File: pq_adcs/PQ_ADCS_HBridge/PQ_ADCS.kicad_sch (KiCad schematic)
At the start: 48 parts, among them J1 CES-110-02-L-S, J10 Pico-Clasp_01x09, J11 Pico-Clasp_01x15, J12 CES-102-02-L-S, J2 CES-110-02-L-S, J3 CES-110-02-L-S, J4 CES-110-02-L-S, J5 Pico-Clasp_01x03, J6 Pico-Clasp_01x10, J7 Pico-Clasp_01x10, J8 Pico-Clasp_01x10, J9 Pico-Clasp_01x10, U1 LPV542, U2 LPV542, U3 LPV542, U4 IIM-42652, U5 DRV8214RTER, U6 TMUX1108RSVR, U7 MMC5983MA

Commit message: H-Bridge Chips Update
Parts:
- added U8, U9: DRV8214RTER, DRV8214RTER:IC_DRV8214RTER, symbol DRV8214RTER:DRV8214RTER
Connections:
- net MAG+X is gone; now on net +MAG+X: J7.2
- net 3V3_PERM: now also U5.16 (VREF), U8.16 (VREF), U8.2 (VCC), U9.16 (VREF), U9.2 (VCC)
- net ADCS_POWER: now also U8.11 (~{SLEEP}), U9.11 (~{SLEEP})
- net GND: now also U5.17 (EXP), U5.3 (RC_OUT), U5.4 (~{FAULT}), U8.12 (PH/IN2), U8.13 (EN/IN1), U8.17 (EXP), U8.3 (RC_OUT), U8.4 (~{FAULT}), U8.7 (GND), U9.12 (PH/IN2), U9.13 (EN/IN1), U9.17 (EXP), U9.3 (RC_OUT), U9.4 (~{FAULT}), U9.7 (GND)
- net SCL3: now also U8.15 (SCL), U9.15 (SCL)
- net SDA3: now also U8.14 (SDA), U9.14 (SDA)
- net +MAG+X: now reaches U5.6 (OUT1)
- net -MAG-X: now reaches U5.8 (OUT2)
- net -MAG-X: now also J6.3
- net MAG+Y renamed +MAG+Y
- net +MAG+Y: now also U8.6 (OUT1)
- net MAG+Z renamed +MAG+Z
- net +MAG+Z: now also U9.6 (OUT1)
- net MAG-X renamed +MAG-X
- net MAG-Y renamed +MAG-Y
- net MAG-Z renamed +MAG-Z
- removed net VCC_MAG: J11.3, J12.1, J6.3, J7.3, J8.3, J9.3
- new net -MAG+X: J7.3
- new net -MAG+Y: J12.1
- new net -MAG+Z: J9.3
- new net -MAG-Y: J11.3, U8.8 (OUT2)
- new net -MAG-Z: J8.3, U9.8 (OUT2)
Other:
- moved on the sheet: U5

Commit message: PCB Update
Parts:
- added R13, R14, R15: 22k, Resistor_SMD:R_0603_1608Metric, symbol Device:R
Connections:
- net 3V3_PERM: now also U5.5 (VM), U8.5 (VM), U9.5 (VM)
- net GND: now also U5.10 (A0), U5.9 (A1), U8.10 (A0), R13.2, R14.2, R15.2
- net at U9.1 (IPROPI): now also R15.1
- net at U8.1 (IPROPI): now also R14.1
- net at U5.1 (IPROPI): now also R13.1
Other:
- note added: "I2C address: 0000b"
- note added: "I2C address: 0001b"
- note added: "I2C address: 0100b"
- note removed: "I2C address:"

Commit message: Reduced errors
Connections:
- net PHT5_ADCS: now also C6.2, R12.1
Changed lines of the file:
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@@
+	(wire
+		(pts
+			(xy 212.09 116.84) (xy 248.92 116.84)
+		)
+		(stroke
+			(width 0)
+			(type default)
+		)
+	)
 	(wire
 		(pts

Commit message: Restart
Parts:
- removed R13, R14, R15: 22k, Resistor_SMD:R_0603_1608Metric, symbol Device:R
- removed U5, U8, U9: DRV8214RTER, DRV8214RTER:IC_DRV8214RTER, symbol DRV8214RTER:DRV8214RTER
- added C11: 100 nF, Capacitor_SMD:C_0603_1608Metric, symbol Device:C
- added C13, C14: 1 uF, Capacitor_SMD:C_0603_1608Metric, symbol Device:C
- added U5: BD2606MVV, Package_DFN_QFN:QFN-16-1EP_4x4mm_P0.65mm_EP2.5x2.5mm, symbol power-nsl:BD2606MVV
- renumbered U1 to U
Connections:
- net -MAG+Y is gone; now on net VCC_MAG: J12.1
- net -MAG+Z is gone; now on net VCC_MAG: J9.3
- net -MAG-X is gone; now on net VCC_MAG: J6.3
- net -MAG-Y is gone; now on net VCC_MAG: J11.3
- net -MAG-Z is gone; now on net VCC_MAG: J8.3
- net ADCS_POWER: now also C11.1, U5.4 (EN), U5.6 (IN)
- net GND: now also C11.2, U5.11 (GND), U5.17 (EPAD)
- net PHT5_ADCS: no longer C6.2, R12.1, U3.7 (OUT_B), U6.9 (S6)
- net SCL3: now also U5.3 (SCL)
- net SDA3: now also U5.2 (SDA)
- net +MAG+X renamed MAG+X
- net MAG+X: now also U5.16 (LEDA2)
- net +MAG+Y renamed MAG+Y
- net MAG+Y: now also U5.12 (LEDC2)
- net +MAG+Z renamed MAG+Z
- net MAG+Z: now also U5.14 (LEDB2)
- net +MAG-X renamed MAG-X
- net MAG-X: now also U5.1 (LEDA1)
- net +MAG-Y renamed MAG-Y
- net MAG-Y: now also U5.13 (LEDC1)
- net +MAG-Z renamed MAG-Z
- net MAG-Z: now also U5.15 (LEDB1)
- net -MAG+X renamed VCC_MAG
- net VCC_MAG: now also U5.5 (OUT)
- new net: C13.1, U5.10 (C2P)
- new net: C13.2, U5.9 (C2N)
- new net: C14.1, U5.8 (C1P)
- new net: C14.2, U5.7 (C1N)
- new net PHT6_ADCS: C6.2, R12.1, U3.7 (OUT_B), U6.9 (S6)
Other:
- note added: "I2C address:"
- note added: "Magnetorquer Actuators"
- note removed: "I2C address: 0000b"
- note removed: "I2C address: 0001b"
- note removed: "I2C address: 0100b"
- note removed: "Magnetorquer H-Bridge Actuators"

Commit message: Great advance
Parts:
- removed C11: 100 nF, Capacitor_SMD:C_0603_1608Metric, symbol Device:C
- removed C13, C14: 1 uF, Capacitor_SMD:C_0603_1608Metric, symbol Device:C
- removed U5: BD2606MVV, Package_DFN_QFN:QFN-16-1EP_4x4mm_P0.65mm_EP2.5x2.5mm, symbol power-nsl:BD2606MVV
- added R13, R14, R15: 22k, Resistor_SMD:R_0603_1608Metric, symbol Device:R
- added U5, U8, U9: DRV8214RTER, DRV8214RTER:IC_DRV8214RTER, symbol DRV8214RTER:DRV8214RTER
- renumbered U to U1
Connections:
- net PHT6_ADCS is gone; now on net PHT5_ADCS: C6.2, R12.1, U3.7 (OUT_B), U6.9 (S6)
- net 3V3_PERM: now also U5.16 (VREF), U5.2 (VCC), U5.5 (VM), U8.16 (VREF), U8.2 (VCC), U8.5 (VM), U9.16 (VREF), U9.2 (VCC), U9.5 (VM)
- net ADCS_POWER: now also U5.11 (~{SLEEP}), U8.11 (~{SLEEP}), U9.11 (~{SLEEP})
- net GND: now also R13.2, R14.2, R15.2, U5.10 (A0), U5.12 (PH/IN2), U5.13 (EN/IN1), U5.17 (EXP), U5.3 (RC_OUT), U5.4 (~{FAULT}), U5.7 (GND), U5.9 (A1), U8.10 (A0), U8.12 (PH/IN2), U8.13 (EN/IN1), U8.17 (EXP), U8.3 (RC_OUT), U8.4 (~{FAULT}), U8.7 (GND), U9.12 (PH/IN2), U9.13 (EN/IN1), U9.17 (EXP), U9.3 (RC_OUT), U9.4 (~{FAULT}), U9.7 (GND)
- net SCL3: now also U5.15 (SCL), U8.15 (SCL), U9.15 (SCL)
- net SDA3: now also U5.14 (SDA), U8.14 (SDA), U9.14 (SDA)
- net MAG+X renamed +MAG+X
- net +MAG+X: now also U5.6 (OUT1)
- net MAG+Y renamed +MAG+Y
- net +MAG+Y: now also U8.6 (OUT1)
- net MAG+Z renamed +MAG+Z
- net +MAG+Z: now also U9.6 (OUT1)
- net MAG-X renamed +MAG-X
- net +MAG-X: now also J7.3
- net MAG-Y renamed +MAG-Y
- net +MAG-Y: now also J12.1
- net MAG-Z renamed +MAG-Z
- net +MAG-Z: now also J9.3
- removed net VCC_MAG: J11.3, J12.1, J6.3, J7.3, J8.3, J9.3
- new net: R15.1, U9.1 (IPROPI)
- new net: R14.1, U8.1 (IPROPI)
- new net: R13.1, U5.1 (IPROPI)
- new net -MAG-X: J6.3, U5.8 (OUT2)
- new net -MAG-Y: J11.3, U8.8 (OUT2)
- new net -MAG-Z: J8.3, U9.8 (OUT2)
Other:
- note added: "I2C address: 0000b"
- note added: "I2C address: 0001b"
- note added: "I2C address: 0100b"
- note added: "Magnetorquer H-Bridge Actuators"
- note removed: "I2C address:"
- note removed: "Magnetorquer Actuators"

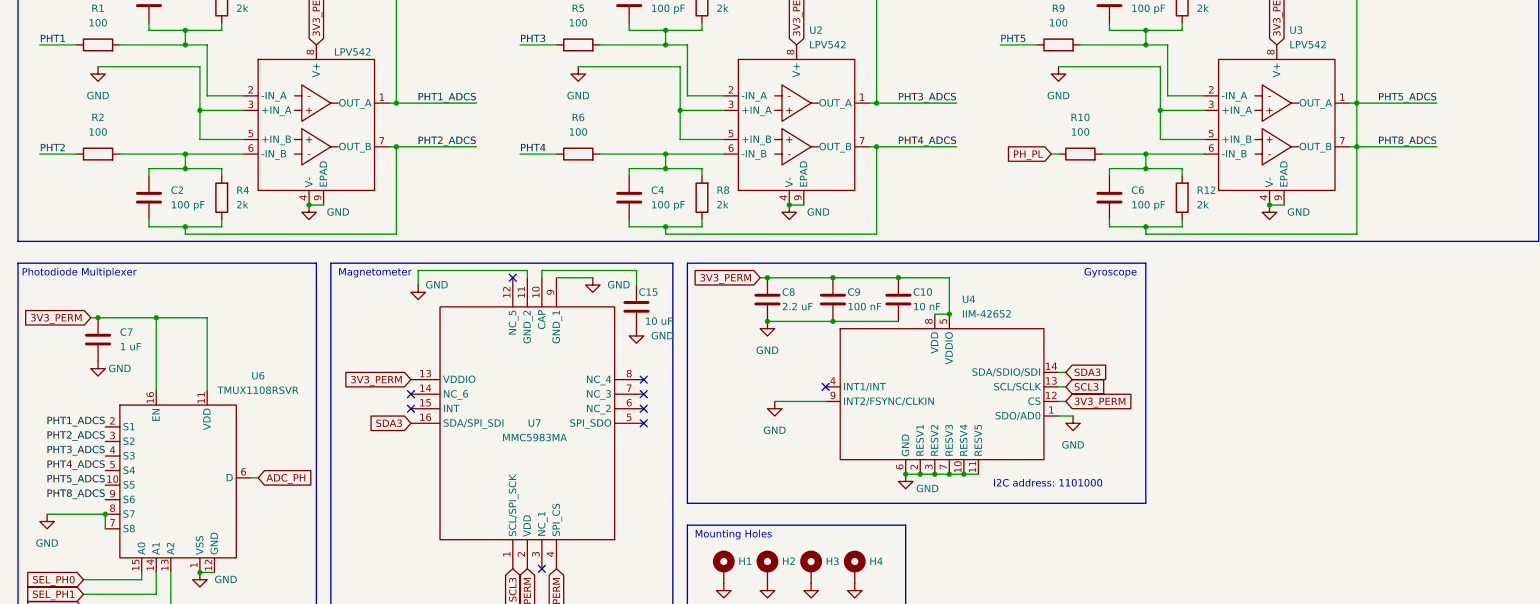
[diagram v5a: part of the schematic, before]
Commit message: No errors, but still warnings
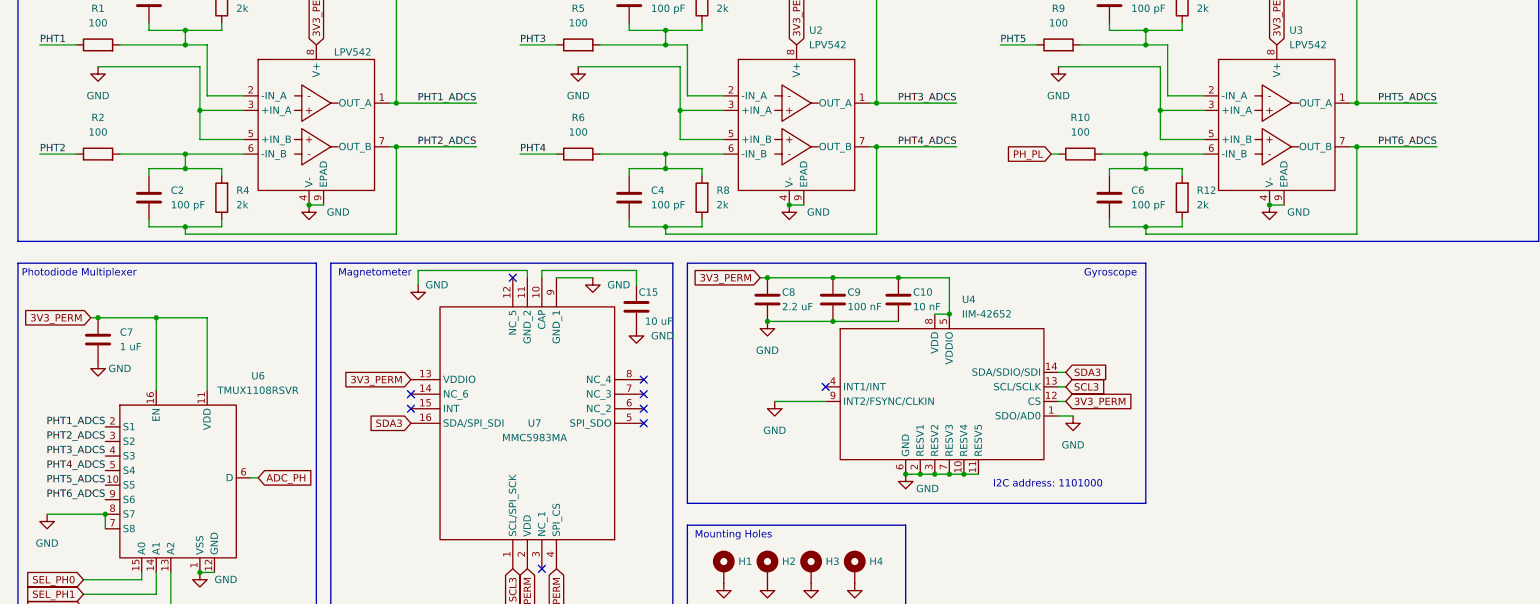
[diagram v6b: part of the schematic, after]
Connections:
- net PHT5_ADCS: no longer C6.2, R12.1, U3.7 (OUT_B), U6.9 (S6)
- new net PHT6_ADCS: C6.2, R12.1, U3.7 (OUT_B), U6.9 (S6)
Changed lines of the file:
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@@
-	(wire
-		(pts
-			(xy 248.92 93.98) (xy 248.92 101.6)
-		)
-		(stroke
-			(width 0)
-			(type default)
-		)
-	)
 	(wire
 		(pts
@@
 		)
 	)
-	(label "PHT8_ADCS"
+	(label "PHT6_ADCS"
 		(at 262.89 101.6 180)
 		(effects
@@
 		)
 	)
-	(label "PHT8_ADCS"
+	(label "PHT6_ADCS"
 		(at 30.48 163.195 180)
 		(effects
